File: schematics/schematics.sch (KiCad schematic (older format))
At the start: 37 parts, among them J1-220V Screw_Terminal_01x02, J2 Screw_Terminal_01x02, J3 Screw_Terminal_01x02, J4 Screw_Terminal_01x02, J5 Screw_Terminal_01x02

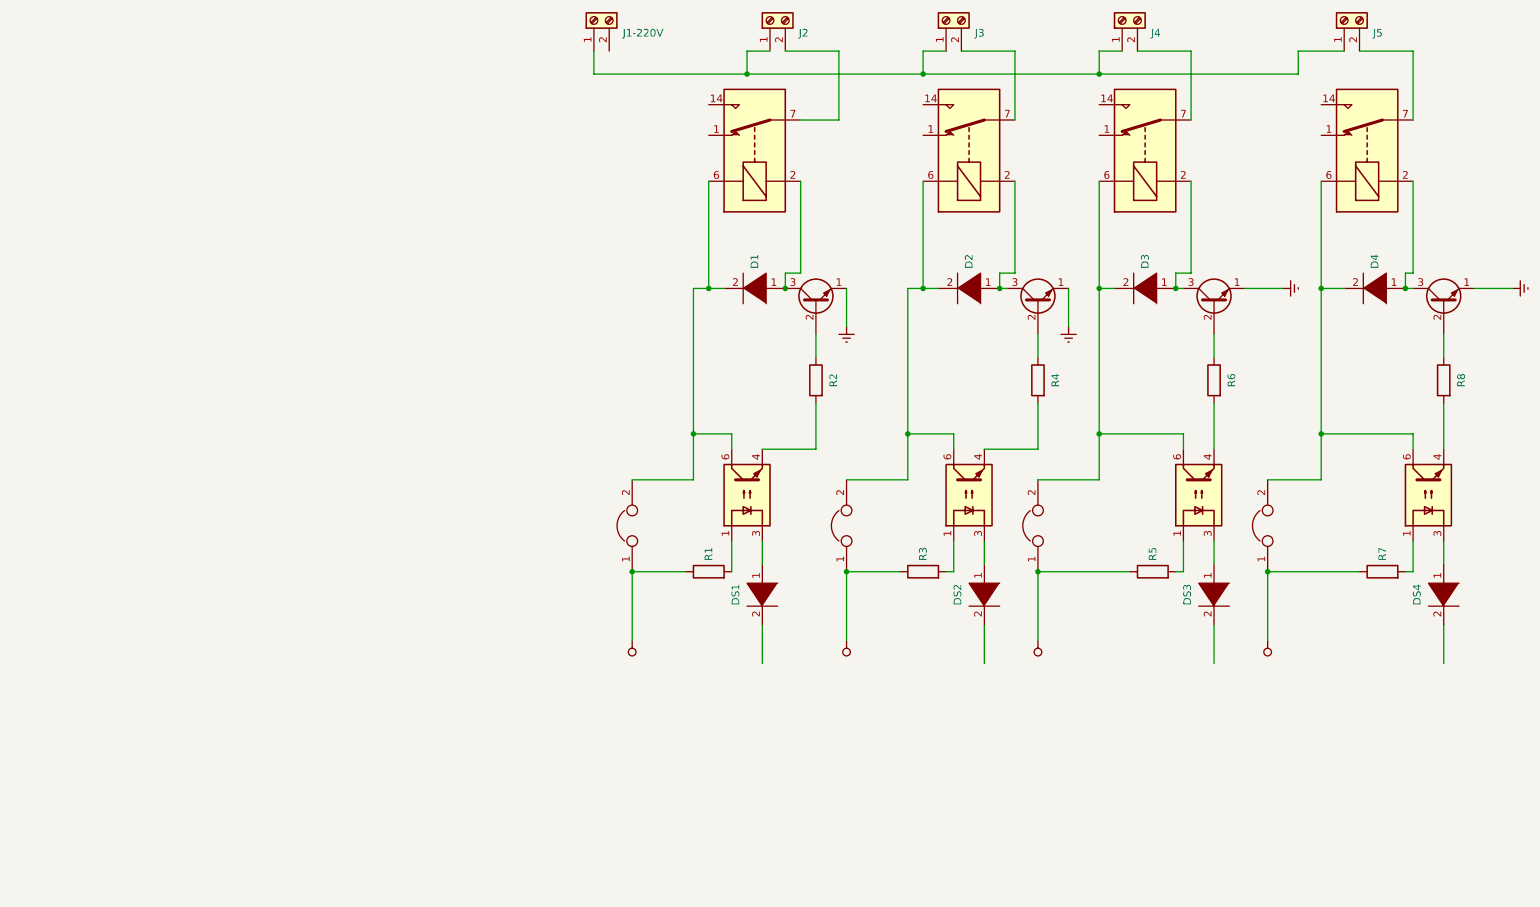
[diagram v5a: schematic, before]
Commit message: Change the names of elements and finalize circuit for the first day
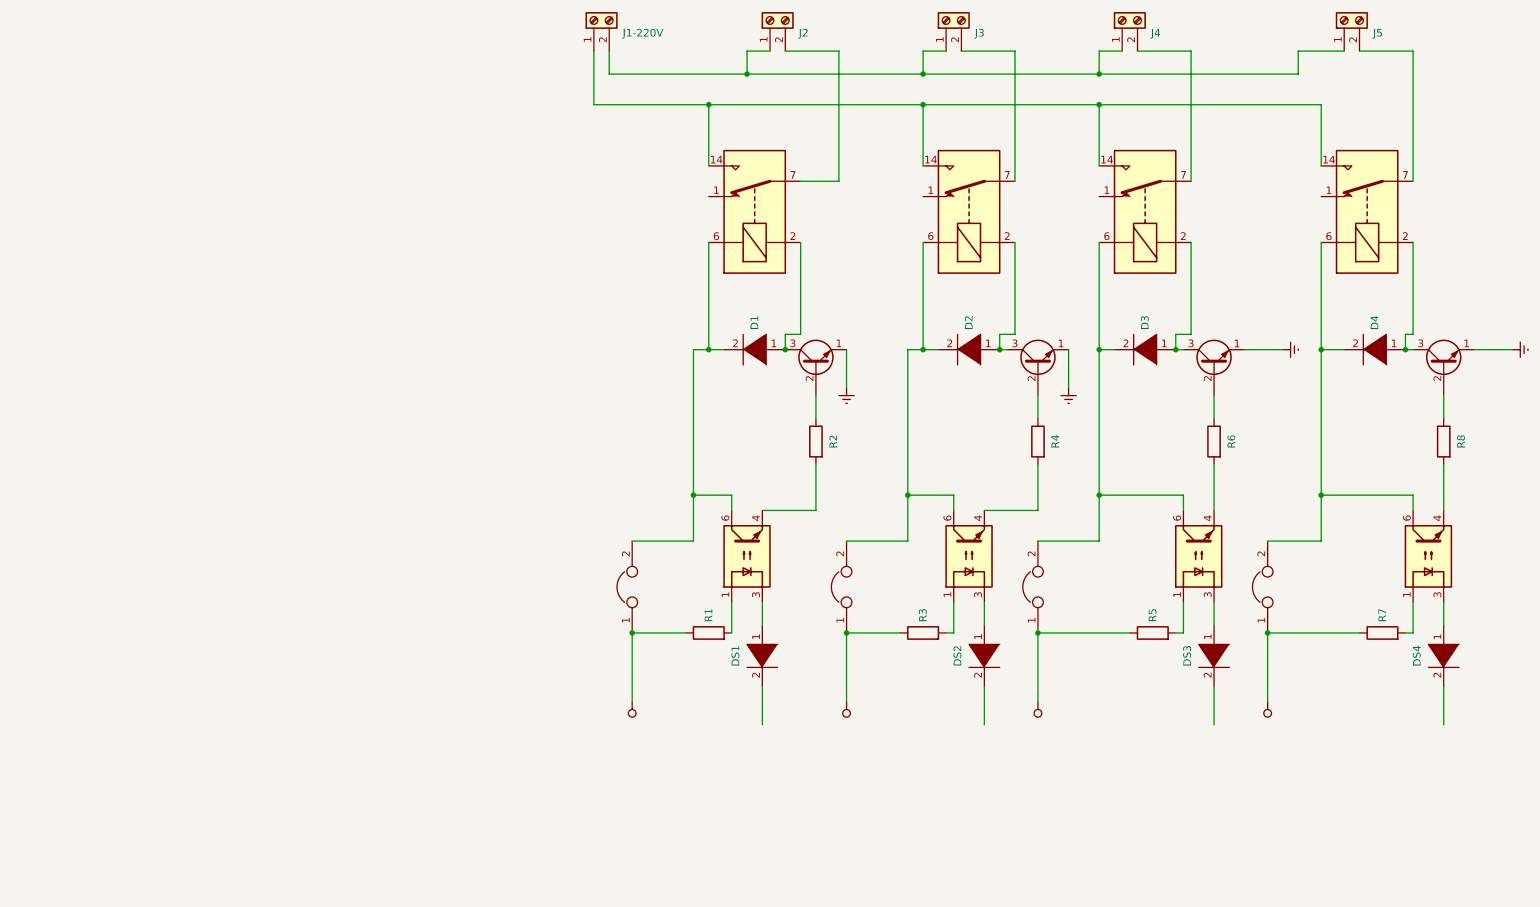
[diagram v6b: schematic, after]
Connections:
- wire segments 104 -> 113
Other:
- moved on the sheet: D1, D2, D3, D4, R1, R2, R3, R4, R5, R6, R7, R8

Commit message: Add buttons and the Arduino
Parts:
- added A?: Arduino_UNO_R3, Module:Arduino_UNO_R3, symbol MCU_Module:Arduino_UNO_R3
- added SW? (x4): SW_Push, symbol Switch:SW_Push
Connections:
- wire segments 113 -> 122
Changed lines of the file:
@@
 Wire Wire Line
 	5100 1500 5100 1850
+$Comp
+L MCU_Module:Arduino_UNO_R3 A?
+U 1 1 5C8D6248
+P 3050 5900
+F 0 "A?" H 3050 7081 50  0001 C CNN
+F 1 "Arduino_UNO_R3" H 3050 6989 50  0001 C CNN
+F 2 "Module:Arduino_UNO_R3" H 3200 4850 50  0001 L CNN
+F 3 "https://www.arduino.cc/en/Main/arduinoBoardUno" H 2850 6950 50  0001 C CNN
+	1    3050 5900
+	1    0    0    -1
+$EndComp
+$Comp
+L Switch:SW_Push SW?
+U 1 1 5C8DB464
+P 1750 3900
+F 0 "SW?" H 1750 4185 50  0000 C CNN
+F 1 "SW_Push" H 1750 4094 50  0000 C CNN
+F 2 "" H 1750 4100 50  0001 C CNN
+F 3 "~" H 1750 4100 50  0001 C CNN
+	1    1750 3900
+	1    0    0    -1
+$EndComp
+$Comp
+L Switch:SW_Push SW?
+U 1 1 5C8E49D7
+P 2400 3900
+F 0 "SW?" H 2400 4185 50  0000 C CNN
+F 1 "SW_Push" H 2400 4094 50  0000 C CNN
+F 2 "" H 2400 4100 50  0001 C CNN
+F 3 "~" H 2400 4100 50  0001 C CNN
+	1    2400 3900
+	1    0    0    -1
+$EndComp
+$Comp
+L Switch:SW_Push SW?
+U 1 1 5C8E9DD3
+P 3000 3900
+F 0 "SW?" H 3000 4185 50  0000 C CNN
+F 1 "SW_Push" H 3000 4094 50  0000 C CNN
+F 2 "" H 3000 4100 50  0001 C CNN
+F 3 "~" H 3000 4100 50  0001 C CNN
+	1    3000 3900
+	1    0    0    -1
+$EndComp
+$Comp
+L Switch:SW_Push SW?
+U 1 1 5C8EEDC9
+P 3550 3900
+F 0 "SW?" H 3550 4185 50  0000 C CNN
+F 1 "SW_Push" H 3550 4094 50  0000 C CNN
+F 2 "" H 3550 4100 50  0001 C CNN
+F 3 "~" H 3550 4100 50  0001 C CNN
+	1    3550 3900
+	1    0    0    -1
+$EndComp
+Wire Wire Line
+	2200 4050 2200 4350
+Wire Wire Line
+	2200 4350 2600 4350
+Connection ~ 2600 4350
+Wire Wire Line
+	2600 4350 3200 4350
+Connection ~ 3200 4350
+Wire Wire Line
+	3200 4350 3750 4350
+Wire Wire Line
+	3750 3900 3750 4350
+Wire Wire Line
+	3200 3900 3200 4350
+Wire Wire Line
+	2600 3900 2600 4350
+Wire Wire Line
+	2200 4050 1950 4050
+Wire Wire Line
+	1950 4050 1950 3900
 $EndSCHEMATC

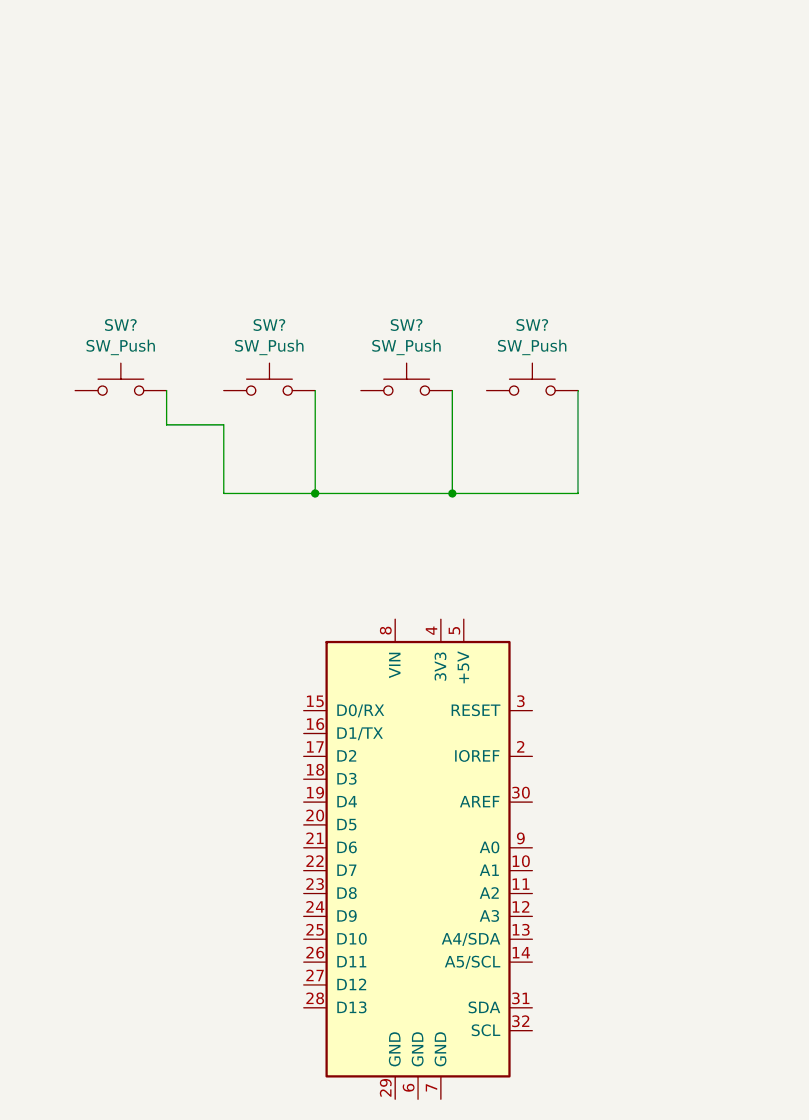
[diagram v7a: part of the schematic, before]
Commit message: Finalize circuit for the buttons
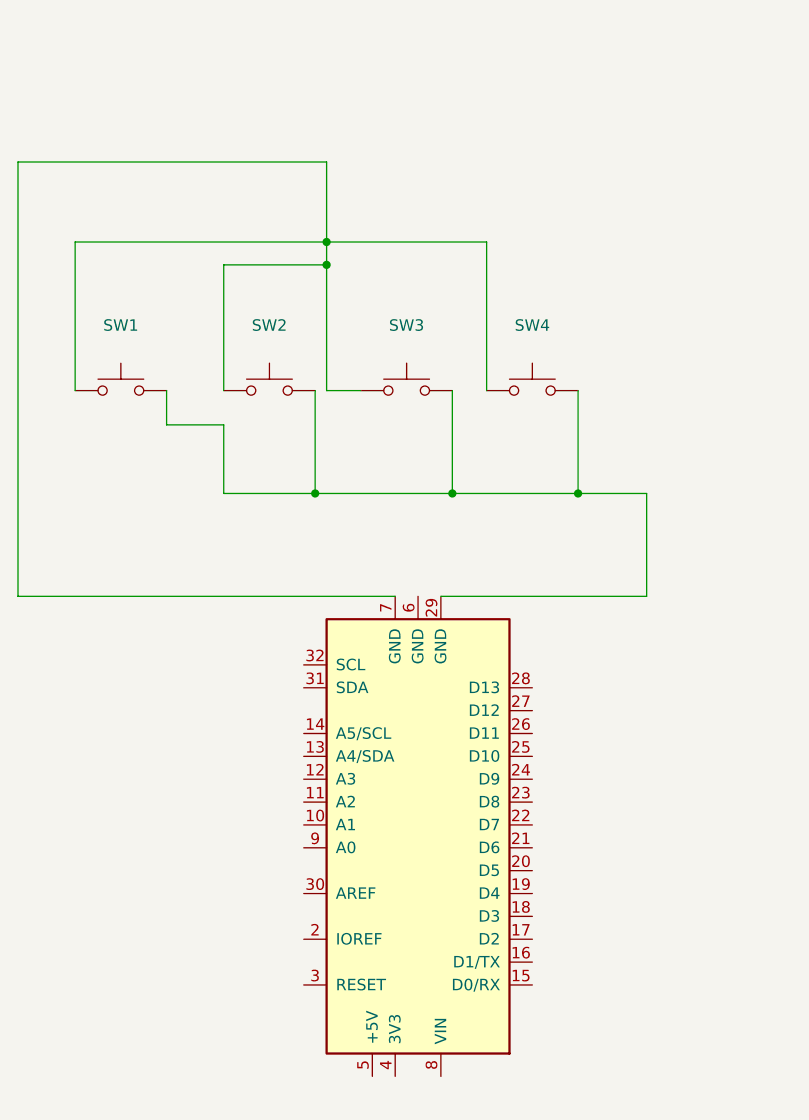
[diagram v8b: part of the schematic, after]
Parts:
- gave numbers to parts that had none: 4
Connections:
- wire segments 122 -> 138
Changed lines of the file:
@@
 F 3 "https://www.arduino.cc/en/Main/arduinoBoardUno" H 2850 6950 50  0001 C CNN
 	1    3050 5900
-	1    0    0    -1
+	-1   0    0    1
 $EndComp
 $Comp
-L Switch:SW_Push SW?
+L Switch:SW_Push SW1
 U 1 1 5C8DB464
 P 1750 3900
-F 0 "SW?" H 1750 4185 50  0000 C CNN
-F 1 "SW_Push" H 1750 4094 50  0000 C CNN
+F 0 "SW1" H 1750 4185 50  0000 C CNN
+F 1 "SW_Push" H 1750 4094 50  0001 C CNN
 F 2 "" H 1750 4100 50  0001 C CNN
 F 3 "~" H 1750 4100 50  0001 C CNN
@@
 $EndComp
 $Comp
-L Switch:SW_Push SW?
+L Switch:SW_Push SW2
 U 1 1 5C8E49D7
 P 2400 3900
-F 0 "SW?" H 2400 4185 50  0000 C CNN
-F 1 "SW_Push" H 2400 4094 50  0000 C CNN
+F 0 "SW2" H 2400 4185 50  0000 C CNN
+F 1 "SW_Push" H 2400 4094 50  0001 C CNN
 F 2 "" H 2400 4100 50  0001 C CNN
 F 3 "~" H 2400 4100 50  0001 C CNN
@@
 $EndComp
 $Comp
-L Switch:SW_Push SW?
+L Switch:SW_Push SW3
 U 1 1 5C8E9DD3
 P 3000 3900
-F 0 "SW?" H 3000 4185 50  0000 C CNN
-F 1 "SW_Push" H 3000 4094 50  0000 C CNN
+F 0 "SW3" H 3000 4185 50  0000 C CNN
+F 1 "SW_Push" H 3000 4094 50  0001 C CNN
 F 2 "" H 3000 4100 50  0001 C CNN
 F 3 "~" H 3000 4100 50  0001 C CNN
@@
 $EndComp
 $Comp
-L Switch:SW_Push SW?
+L Switch:SW_Push SW4
 U 1 1 5C8EEDC9
 P 3550 3900
-F 0 "SW?" H 3550 4185 50  0000 C CNN
-F 1 "SW_Push" H 3550 4094 50  0000 C CNN
+F 0 "SW4" H 3550 4185 50  0000 C CNN
+F 1 "SW_Push" H 3550 4094 50  0001 C CNN
 F 2 "" H 3550 4100 50  0001 C CNN
 F 3 "~" H 3550 4100 50  0001 C CNN
@@
 Wire Wire Line
 	1950 4050 1950 3900
+Wire Wire Line
+	3750 4350 4050 4350
+Wire Wire Line
+	4050 4350 4050 4800
+Wire Wire Line
+	4050 4800 3150 4800
+Connection ~ 3750 4350
+Wire Wire Line
+	1550 3900 1550 3250
+Wire Wire Line
+	3350 3900 3350 3250
+Wire Wire Line
+	1550 3250 2650 3250
+Wire Wire Line
+	2200 3900 2200 3350
+Wire Wire Line
+	2650 3350 2650 3250
+Wire Wire Line
+	2200 3350 2650 3350
+Connection ~ 2650 3250
+Wire Wire Line
+	2650 3250 3350 3250
+Wire Wire Line
+	2800 3900 2650 3900
+Wire Wire Line
+	2650 3900 2650 3350
+Connection ~ 2650 3350
+Wire Wire Line
+	2650 3250 2650 2900
+Wire Wire Line
+	2650 2900 1300 2900
+Wire Wire Line
+	1300 2900 1300 4800
+Wire Wire Line
+	1300 4800 2950 4800
 $EndSCHEMATC
